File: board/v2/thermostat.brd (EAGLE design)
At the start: 37.5 x 36.2 mm, 18 parts, among them IC1 7805TV, Q1 MOSFET-NCHANNEL2N7000, Q2 MOSFET-NCHANNEL2N7000, Q3 MOSFET-NCHANNEL2N7000

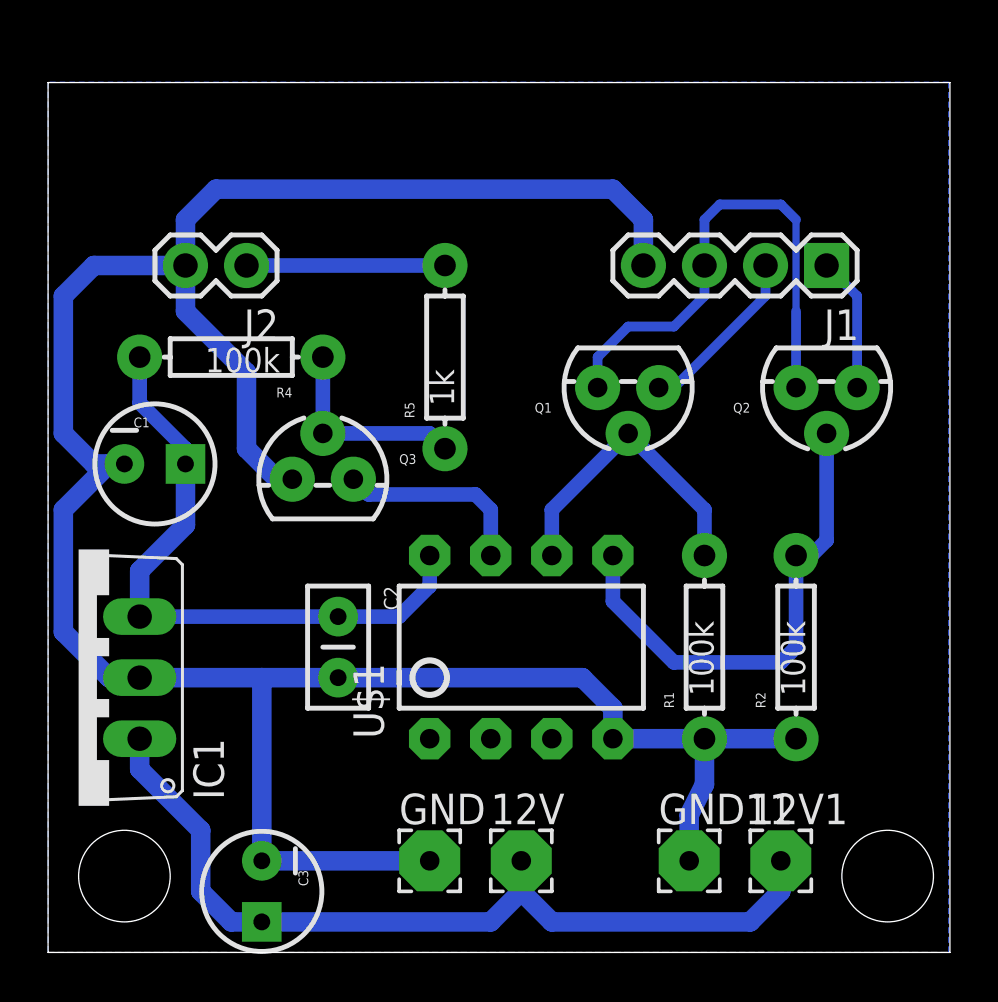
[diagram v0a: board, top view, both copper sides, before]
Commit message: SMD layout complete
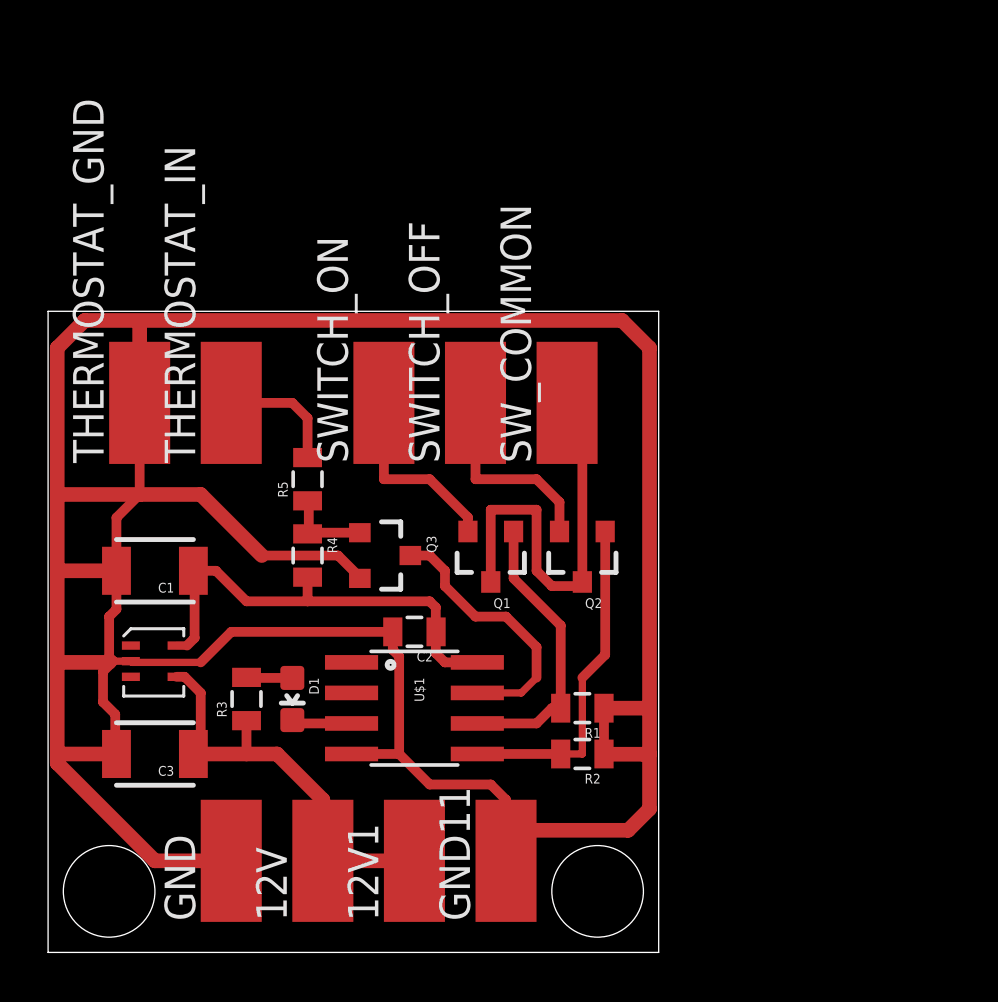
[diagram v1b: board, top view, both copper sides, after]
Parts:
- removed IC1: 7805TV, linear:TO220V
- removed J1: (no value), SparkFun-Connectors:1X04
- removed J2: (no value), SparkFun-Connectors:1X02
- added D1: (no value), SparkFun-LED:LED-0603
- added R3: 680, SparkFun-Passives:0805
- added SWITCH_OFF, SWITCH_ON, SW_COMMON, THERMOSTAT_GND, THERMOSTAT_IN: (no value), wirepad:SMD2,54-5,08
- added TPS71550DCKR: (no value), Synapseware:SC70-5
- 12V, 12V1, GND, GND11: value (none) -> WIREPADSMD2,54-5,08; device wirepad:2,54/0,8 -> wirepad:SMD2,54-5,08
- C1: device SparkFun-Capacitors:CPOL-RADIAL-10UF-25V -> SparkFun-Capacitors:1210
- C2: device SparkFun-Capacitors:CAP-PTH-SMALLEZ -> SparkFun-Capacitors:0805
- C3: value 0.1uF -> 1uF; device SparkFun-Capacitors:CPOL-RADIAL-10UF-25V -> SparkFun-Capacitors:1210
- Q1, Q2, Q3: value MOSFET-NCHANNEL2N7000 -> MOSFET-NCHANNELAO3404A; device SparkFun-DiscreteSemi:TO-92 -> SparkFun-DiscreteSemi:SOT23-3
- R1, R2, R4, R5: device SparkFun-Passives:AXIAL-0.3 -> SparkFun-Passives:0805
- U$1: value ATTINY13DIP -> ATTINY13SOIC; device SparkFun-DigitalIC:DIP08 -> SparkFun-DigitalIC:SO08
- moved 12V1 15.2 mm to (15.2, 3.81)
- moved Q2 12.3 mm to (22.2, 16.5)
- moved R2 9.94 mm to (22.2, 8.26), turned to 180 degrees
- moved Q1 9.03 mm to (18.4, 16.5)
- moved R4 8.84 mm to (10.8, 16.5), turned to 270 degrees
- moved 12V 8.25 mm to (11.4, 3.81)
- moved GND 8.25 mm to (7.62, 3.81)
- moved R5 7.65 mm to (10.8, 19.7)
- moved GND11 7.62 mm to (19.1, 3.81)
- moved C3 7.24 mm to (4.45, 8.26), turned to 180 degrees
- moved R1 5.68 mm to (22.2, 10.2), turned to 180 degrees
- moved U$1 5.12 mm to (15.2, 10.2), turned to 270 degrees
- moved C1 4.45 mm to (4.45, 15.9), turned to 180 degrees
- moved Q3 4.07 mm to (14.0, 16.5), turned to 270 degrees
- moved C2 3.24 mm to (15.2, 13.3), turned to 180 degrees
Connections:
- new net LED: D1.C, U$1.3
- new net N$2: D1.A, R3.2
- net 12V: now also R3.1, TPS71550DCKR.4; no longer IC1.1
- net 5V: now also R4.2, TPS71550DCKR.5; no longer IC1.3, R4.P$2
- net GND: now also Q3.2, R1.1, R2.1, THERMOSTAT_GND.1, TPS71550DCKR.2; no longer IC1.2, J1.4, J2.2, Q3.1, R1.P$1, R2.P$1
- net HEAT_OFF: now also Q2.1, R2.2; no longer Q2.2, R2.P$2
- net HEAT_ON: now also Q1.1, R1.2; no longer Q1.2, R1.P$2
- net N$1: now also Q3.1, R4.1, R5.1; no longer Q3.2, R4.P$1, R5.P$1
- net SWITCH_OFF: now also Q2.2, SWITCH_OFF.1; no longer J1.1, Q2.1
- net SWITCH_ON: now also Q1.2, SWITCH_ON.1; no longer J1.2, Q1.1
- net SW_COMMON: now also SW_COMMON.1; no longer J1.3
- net THERMOSTAT_IN: now also R5.2, THERMOSTAT_IN.1; no longer J2.1, R5.P$2
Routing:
- net GND: track 110.7 -> 137.7 mm
- net 12V: track 36.2 -> 17.9 mm
- net 5V: track 26.2 -> 19.2 mm
- net HEAT_OFF: track 20.6 -> 14.0 mm
- net N$1: track 8.52 -> 3.54 mm
- net SW_COMMON: track 21.3 -> 17.2 mm
- net THERMOSTAT_IN: track 8.26 -> 5.08 mm
- net SENSOR_IN: track 8.15 -> 11.2 mm
- net SWITCH_OFF: track 5.61 -> 8.29 mm
- net LED: track 0.00 -> 2.53 mm
- net N$2: track 0.00 -> 1.91 mm
- net N$6: track 0.00 -> 1.91 mm
- net N$5: track 0.00 -> 1.91 mm
- net N$4: track 0.00 -> 1.91 mm
- net N$7: track 0.00 -> 1.27 mm
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- removed copper zone on layer 16, net N$2
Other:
- board size 37.5 x 36.2 mm -> 25.4 x 26.7 mm
